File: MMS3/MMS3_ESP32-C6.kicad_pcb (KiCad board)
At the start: 4 copper layers, 100 x 50 mm, 189 parts, among them J1 86093488324755V1LF, J2 AMASS XT60, J4 USB_C_Receptacle_USB2.0_16P, J5 Conn_Coaxial, J7 AMASS XT60, J8 RJ45_LED_Shielded, J9 RJ45_LED_Shielded, Q1 MMBT3904 100-300, Q2 MMBT3904 100-300, SW1 SK12D07VG5, SW3 TC-6615Z-12.5-260, U1 TJA1044GTK_3Z, U10 AT24C256C, U11 ESP32-C6_C5364646, U12 TCA9555RTWR, U13 CH340G, U15 AMS1117-3.3, U2 TPS54560BDDA, U3 FSUSB42UMX, U302 CH334P, U4 TPD2EUSB30DRTR-TP, U5 TPD2EUSB30DRTR-TP, U6 TJA1044GTK_3Z, U7 FSUSB42UMX, U8 ZD25Q128CSIGT, U9 TPD2EUSB30DRTR-TP, X2 40MHz, 15pF, X3 X322512MSB4SI, Y900 Crystal_GND24

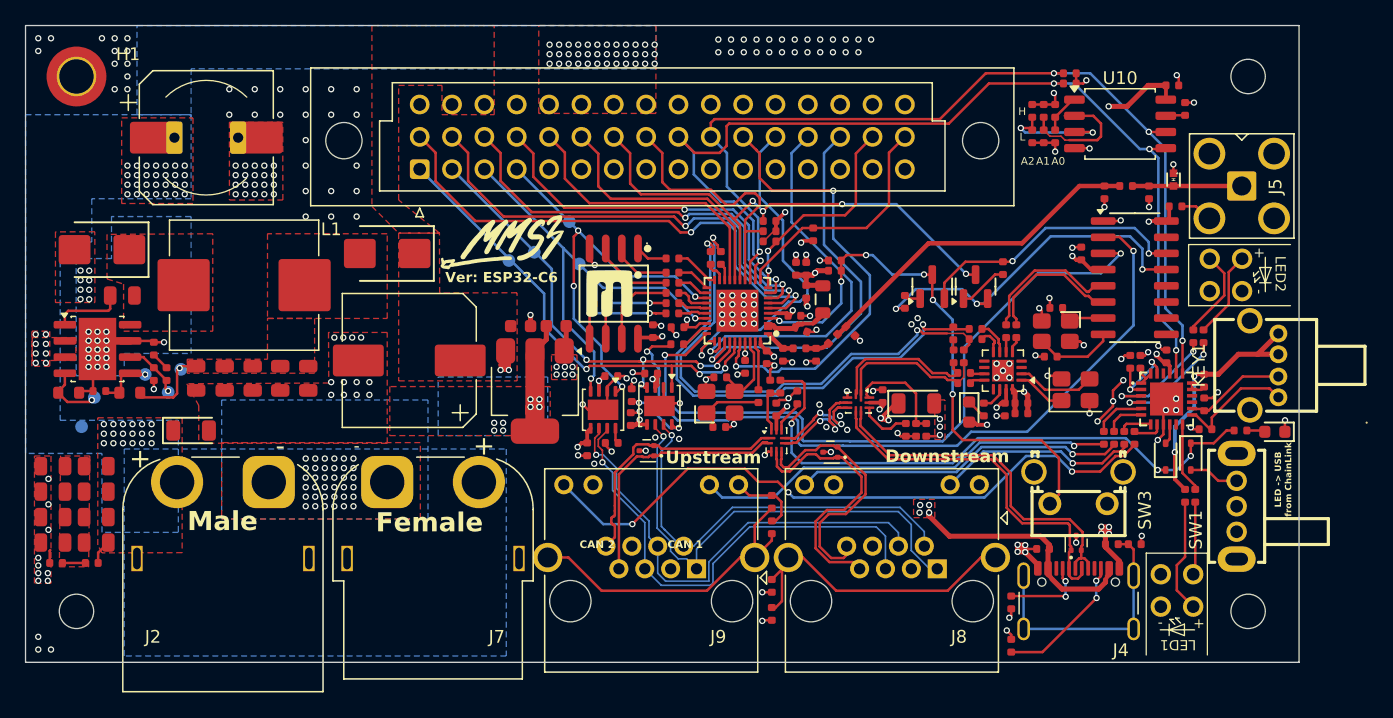
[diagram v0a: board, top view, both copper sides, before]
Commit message: fixed swapped RX/TX & D+/D_
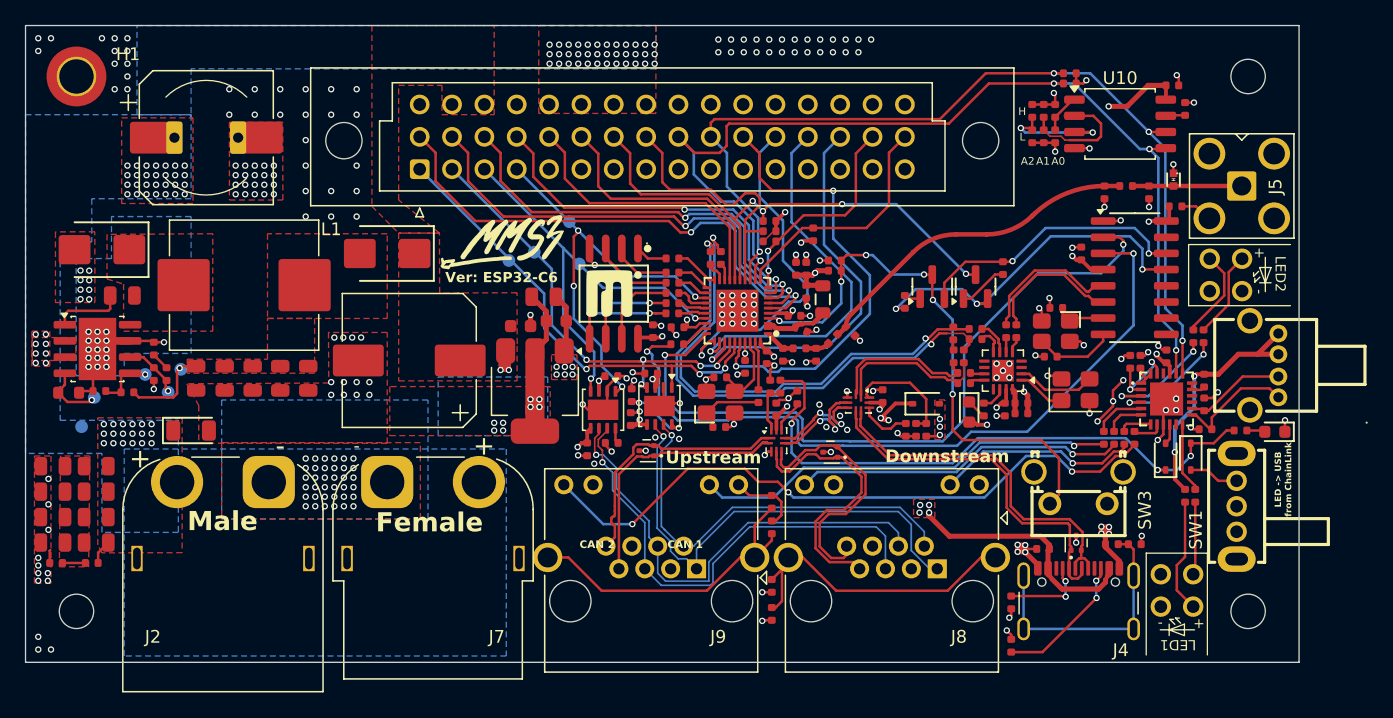
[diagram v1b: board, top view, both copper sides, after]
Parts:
- removed D5: SM4007PL, PCM_JLCPCB:D_SOD-123FL
- removed R36: 43kΩ, PCM_JLCPCB:R_0603
- added C48: 22uF, PCM_JLCPCB:C_0805, F.Cu at (139.7, 103.3)
- added D9: 1N5819WS, PCM_JLCPCB:D_SOD-323, F.Cu at (169.7, 111.7)
- added R21: 47kΩ, PCM_JLCPCB:R_0402, F.Cu at (107.0, 110.8)
- L3: footprint PCM_JLCPCB:C_0402 -> PCM_JLCPCB:L_0402
- moved R50 0.80 mm to (152.8, 100.2)
- moved R51 0.80 mm to (153.6, 100.2)
- moved C10 0.40 mm to (140.7, 105.2)
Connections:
- R49 pad 1: /ESP32-C6/UART0.TX -> /ESP32-C6/UART0.RX
- R50 pad 1: /ESP32-C6/GPIO12 -> /ESP32-C6/GPIO13
- R51 pad 1: /ESP32-C6/GPIO13 -> /ESP32-C6/GPIO12
- U11 pad 30: /ESP32-C6/UART0.RX -> /ESP32-C6/UART0.TX
- U2 pad 3: BRD_VIN -> unconnected-(U2-EN-Pad3)
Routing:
- net +3V3: track 253.8 -> 256.1 mm
- net GND: track 104.7 -> 107.0 mm, vias 275 -> 273
- net /ESP32-C6/UART0.RX: track 56.4 -> 58.6 mm
- net /ESP32-C6/UART0.TX: track 59.0 -> 57.8 mm
- net +5V: track 106.8 -> 107.9 mm
- net /ESP32-C6/USB.D-: track 39.8 -> 39.1 mm
- net Net-(C41-Pad1): track 6.47 -> 7.13 mm
- net /ESP32-C6/More_RF: track 27.0 -> 26.4 mm
- net Net-(U7-SEL): track 8.37 -> 8.92 mm
